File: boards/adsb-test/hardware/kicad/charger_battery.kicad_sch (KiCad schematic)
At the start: 42 parts, among them J301 2S Li-ion pack (BAT+, GND, NT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, U301 BQ25798, U302 MCP1703 3.0V (2 uA Iq)

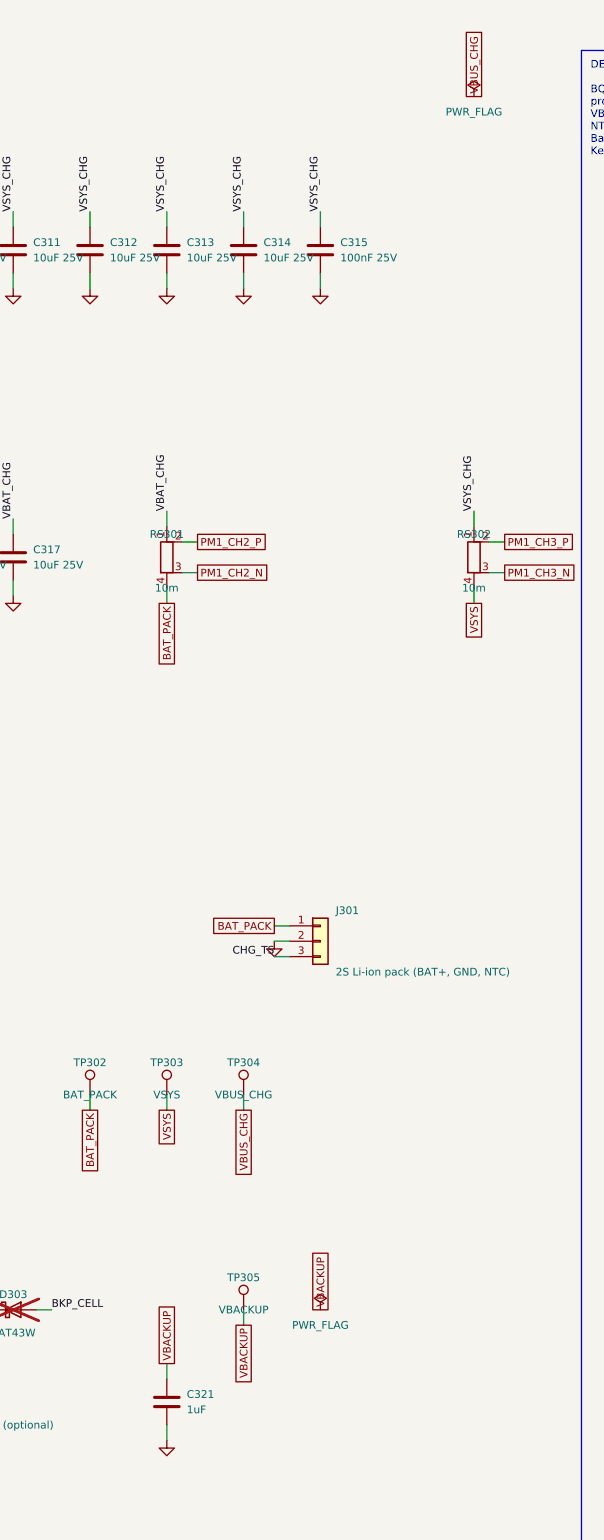
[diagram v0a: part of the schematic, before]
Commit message: ADSB_Test: User USB-C on its own sheet, RP2040 GPIO header + optional I2C, shunt/PWR_FLAG text fixed
Co-Authored-By: Claude Opus 5.5 <noreply@anthropic.com>
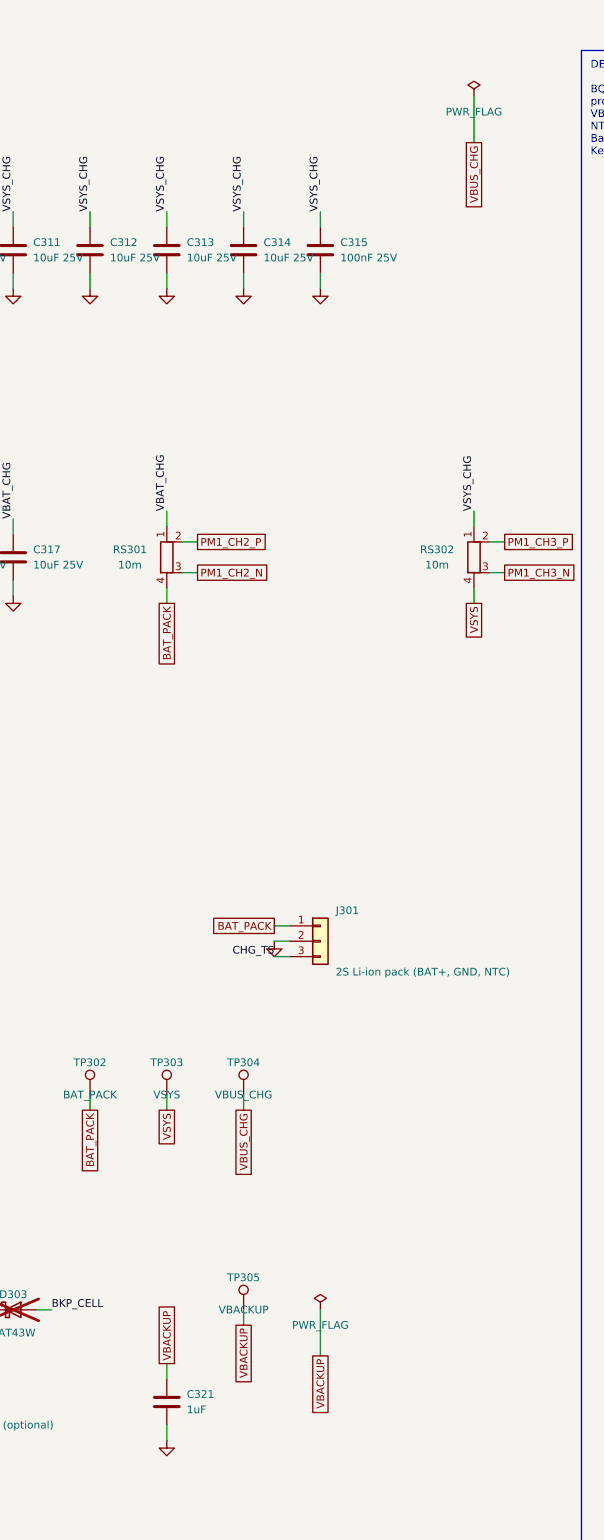
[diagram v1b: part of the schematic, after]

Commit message: ADSB_Test: Dev port split over three A3 sheets; old note boxes replaced with short current notes
Co-Authored-By: Claude Opus 5.5 <noreply@anthropic.com>
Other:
- note added: "CHARGER: BQ25798 buck-boost 2S charger + power path (I2C 0x6B), PROG 8.2k = 2S / 750 kHz, TS divider 5.23k/30.1k (10k NTC). Pack: 2 x 18650 with its own 2S protection + balancing on J301. RS301 VBAT (PM1 CH2, bidirectional), RS302 VSYS (PM1 CH3). VBACKUP: MCP1703 3.0 V (2 uA) from VSYS -> BAT43W -> P4 RTC_VBAT and GPS V_BCKP; optional CR1220 BT301 (DNP)."

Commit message: ADSB_Test: Kelvin shunt footprint, Wi-Fi RP-SMA on the top edge, PCB parity 0
- Shunts RS201-RS409: 4-pad R_Shunt_1206_Kelvin_HandSolder (net-tied sense
  pads) replaces the 2-pad 1206, which put the sense net on the load pad.
- Wi-Fi: module IPEX -> U.FL jumper -> J601 -> J602 RP-SMA on the top long
  edge, away from the 1090/978 and GNSS SMAs. BOM, datasheets, docs.
- gen_pcb: symbol fields and BOM flags copied to footprints, unconnected
  net names escaped; top-edge placement.

Co-Authored-By: Claude Opus 5.5 <noreply@anthropic.com>
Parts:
- RS301, RS302: footprint Resistor_SMD:R_1206_3216Metric_Pad1.30x1.75mm_HandSolder -> ADSB_Test:R_Shunt_1206_Kelvin_HandSolder; Check Kelvin-route pins 2/3 to the PAC1954 -> Route sense pads 2/3 to the PAC1954 as a pair

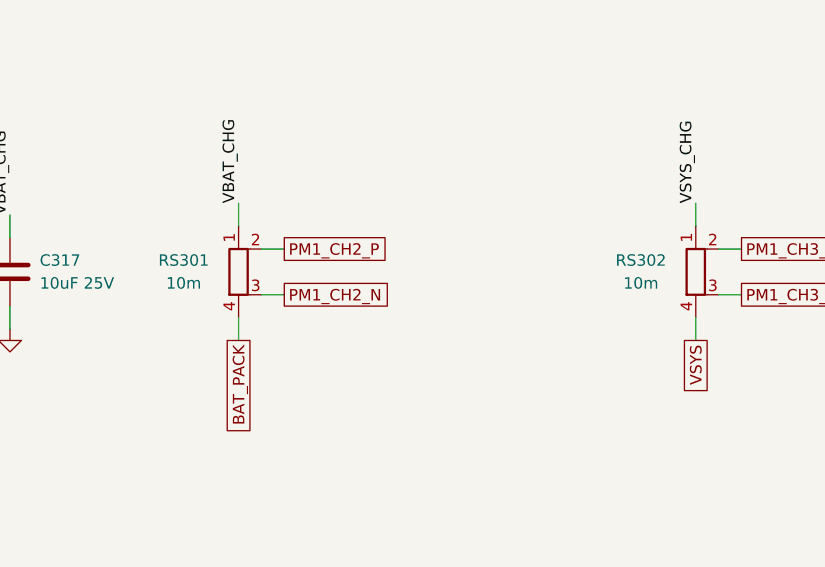
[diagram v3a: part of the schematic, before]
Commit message: ADSB_Test: current shunts resized for the PAC1954 100 mV range
Each shunt now gives ~40-75 mV at its rail's expected peak (several light
rails gave 2-20 mV): battery/VSYS 20m, 3V3 total 30m, 5V_SDR 50m, 3V3_SD
330m, 3V3_ETH 1R, m1421 and 3V3_PERIPH 2.2R. Full-scale currents on the
Power Monitor sheet, BOM updated, PCB regenerated (user's KiCad moves
captured into PLACE first; nothing moved, parity 0).

Co-Authored-By: Claude Opus 5.5 <noreply@anthropic.com>
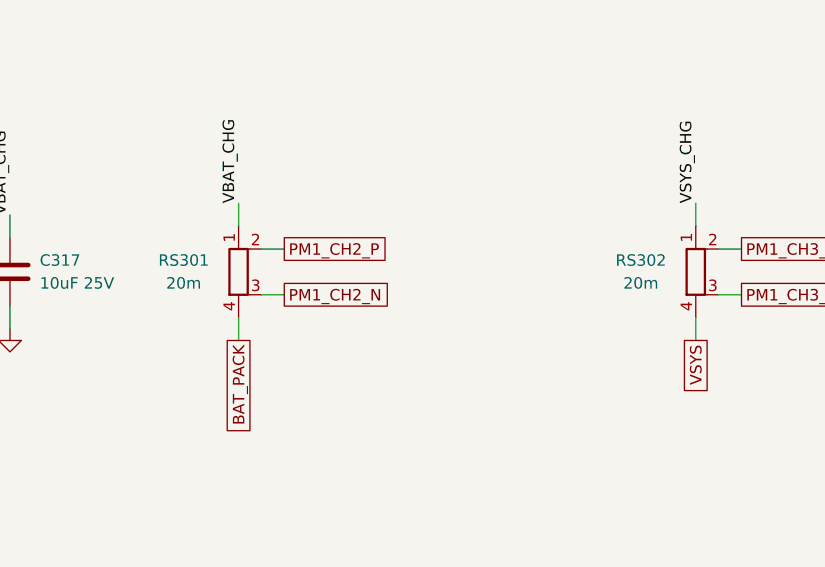
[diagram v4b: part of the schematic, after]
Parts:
- RS301, RS302: value 10m -> 20m
